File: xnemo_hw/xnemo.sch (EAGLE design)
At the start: 13 parts, among them J1 MICRO_USB_B_RECEPT, U1 LTC4O88, U2 L3GD20, U3 STM32F405RG, U5 HMC5883L, U6 ADXL345, X1 TXC_7A_XTAL

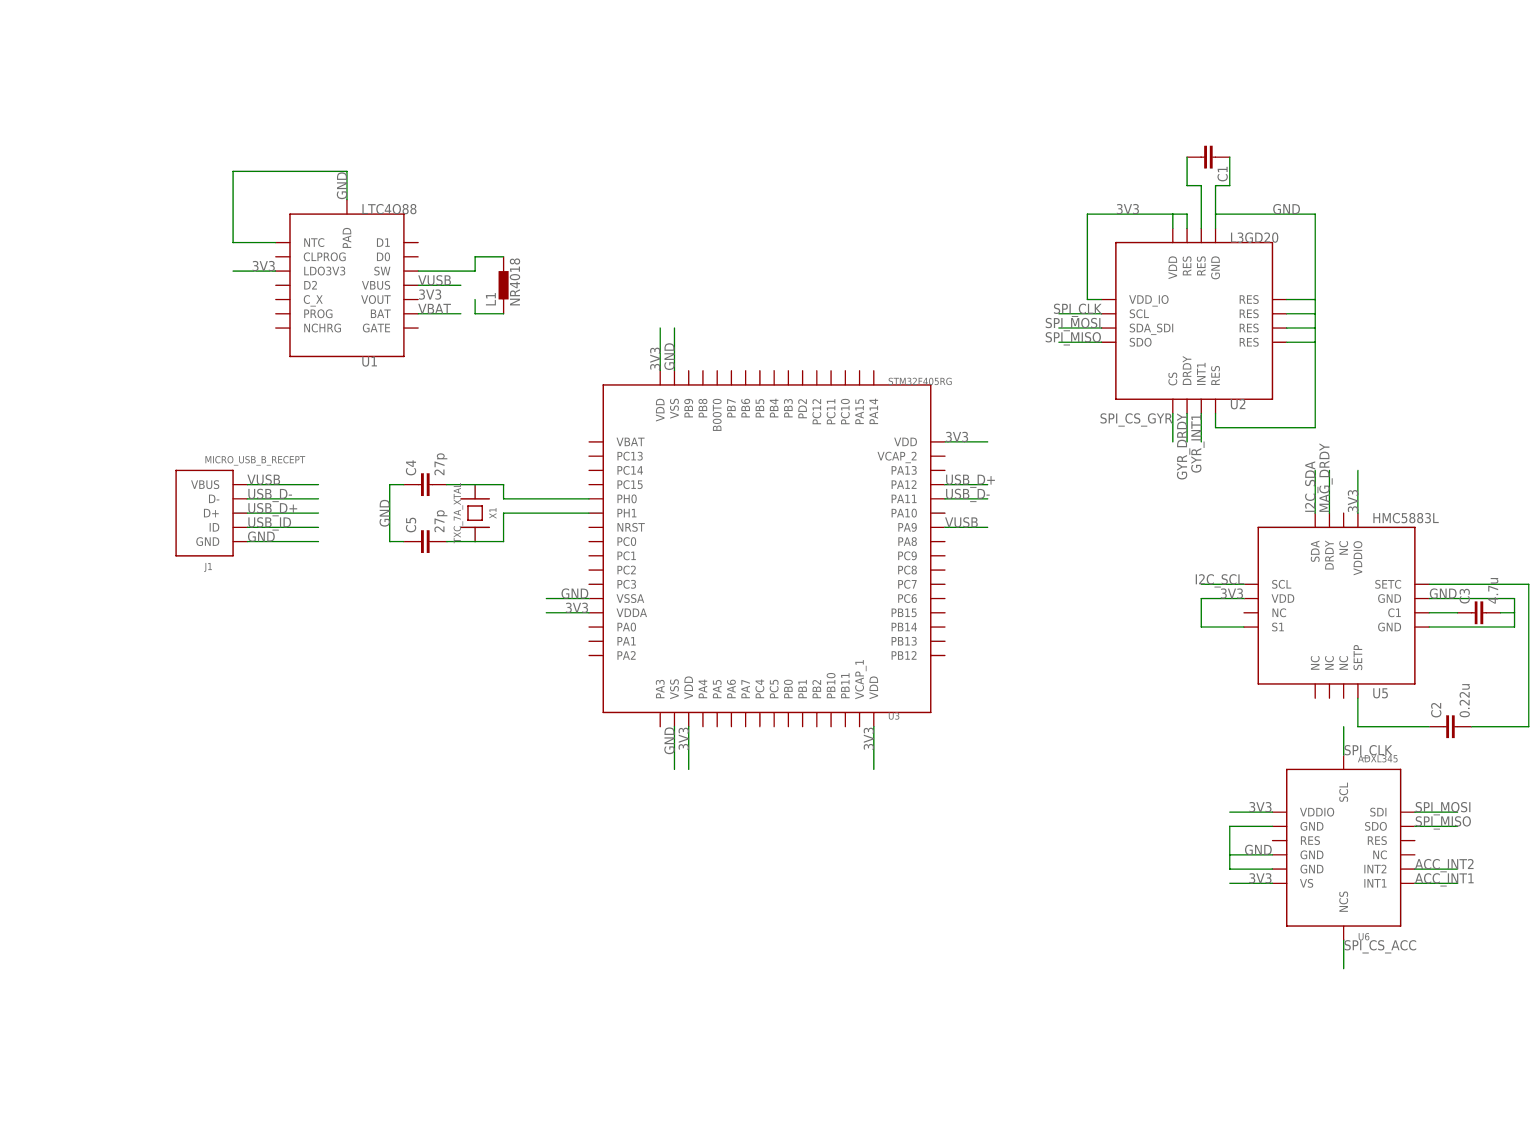
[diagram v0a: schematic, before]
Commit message: Updated schematic to all essential connections, started board to make smarter pin selections by including routing considerations
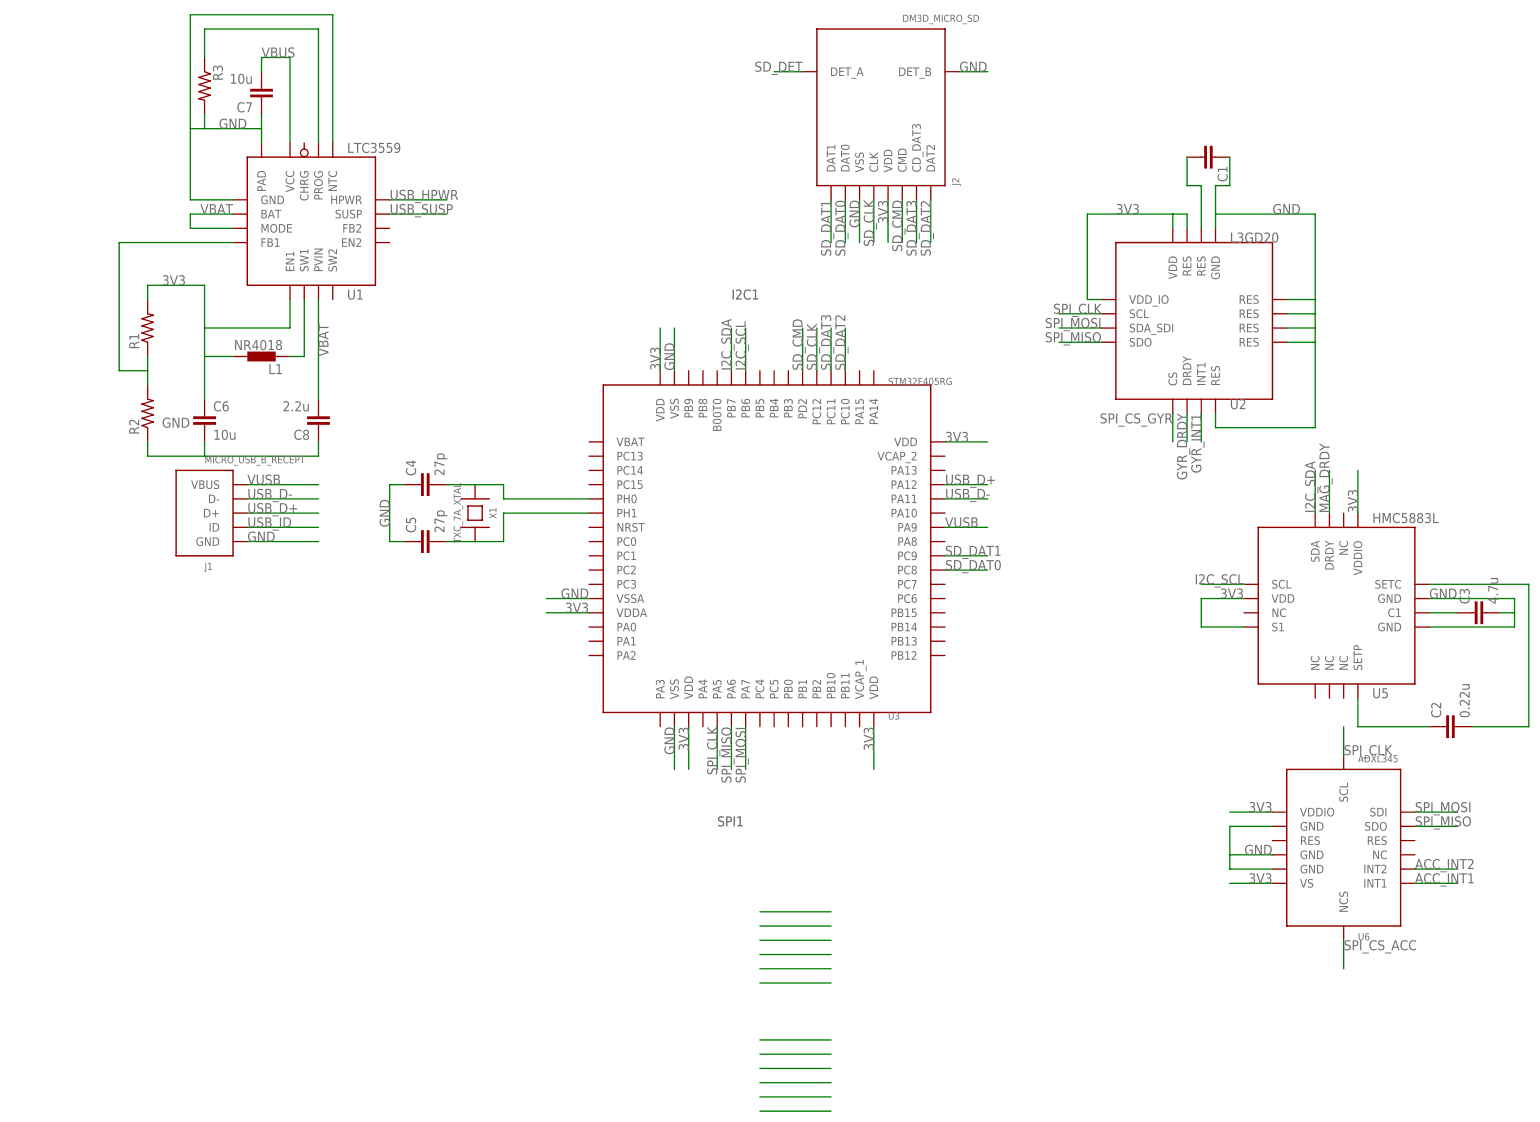
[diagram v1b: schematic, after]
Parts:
- added C6, C7: 10u, resistor:C-EUC0805
- added C8: 2.2u, resistor:C-EUC0805
- added J2: DM3D_MICRO_SD, xnemo:DM3D_MICRO_SD
- added R1, R2, R3: (no value), resistor:R-US_R0402
- U1: value LTC4O88 -> LTC3559; device xnemo:LTC4O88 -> xnemo:LTC3559
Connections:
- removed net SW: L1.2, U1.SW
- new net BUCK_FB1: R1.1, R2.2, U1.FB1
- new net BUCK_SW1: L1.1, U1.SW1
- new net N$1: R3.1, U1.PROG
- new net SD_CLK: J2.CLK, U3.PC12
- new net SD_CMD: J2.CMD, U3.PD2
- new net SD_DAT0: J2.DAT0, U3.PC8
- new net SD_DAT1: J2.DAT1, U3.PC9
- new net SD_DAT2: J2.DAT2, U3.PC10
- new net SD_DAT3: J2.CD_DAT3, U3.PC11
- new net SD_DET: J2.DET_A
- new net USB_HPWR: U1.HPWR
- new net USB_SUSP: U1.SUSP
- new net VBUS: C7.2, U1.VCC
- net 3V3: now also C6.1, J2.VDD, L1.2, R1.2, U1.EN1; no longer L1.1, U1.LDO3V3
- net GND: now also C6.2, C7.1, C8.1, J2.DET_B, J2.VSS, R2.1, R3.2, U1.GND
- net I2C_SCL: now also U3.PB6
- net I2C_SDA: now also U3.PB7
- net SPI_CLK: now also U3.PA5
- net SPI_MISO: now also U3.PA6
- net SPI_MOSI: now also U3.PA7
- net VBAT: now also C8.2, U1.MODE, U1.PVIN
- net VUSB: no longer U1.VBUS
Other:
- note added: "I2C1"
- note added: "SPI1"
- moved on the sheet: L1

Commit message: Updated some little things and added JTAG header
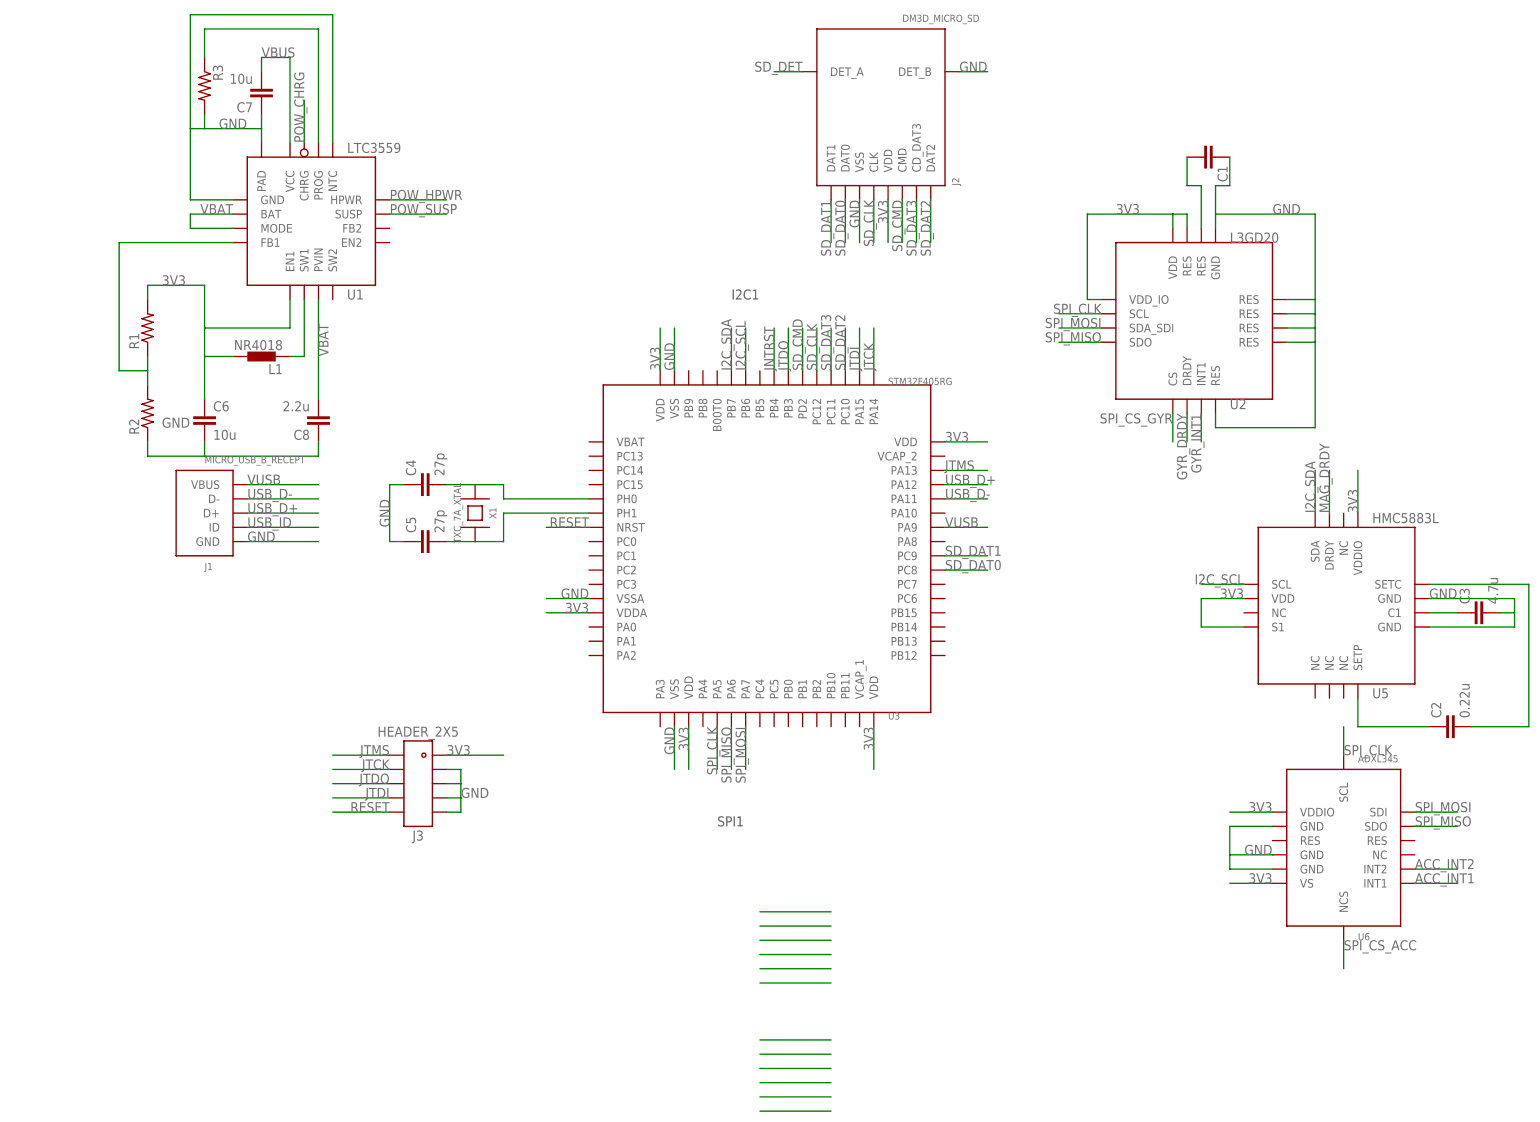
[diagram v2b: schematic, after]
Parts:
- added J3: HEADER_2X5, xnemo:HEADER_2X5
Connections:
- net USB_HPWR renamed POW_HPWR
- net USB_SUSP renamed POW_SUSP
- new net JNTRST: U3.PB4
- new net JTCK: J3.4, U3.PA14
- new net JTDI: J3.8, U3.PA15
- new net JTDO: J3.6, U3.PB3
- new net JTMS: J3.2, U3.PA13
- new net POW_CHRG: U1.CHRG
- new net RESET: J3.10, U3.NRST
- net 3V3: now also J3.1
- net GND: now also J3.3, J3.5, J3.7, J3.9

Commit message: Started bord
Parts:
- added C10, C11, C12, C9: 2.2u, resistor:C-EUC0603
- C4, C5: device resistor:C-EUC0603 -> resistor:C-EUC0402
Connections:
- net N$5 renamed GYR_RES
- removed net VBUS: C7.2, U1.VCC
- new net N$17: C10.1, U3.VCAP_1
- new net N$5: C11.1, U3.VCAP_2
- net 3V3: now also C12.1, C9.2
- net ACC_INT1: now also U3.PB1
- net ACC_INT2: now also U3.PB0
- net GND: now also C10.2, C11.2, C12.2, C9.1
- net GYR_DRDY: now also U3.PB13
- net GYR_INT1: now also U3.PB12
- net POW_CHRG: now also U3.PB2
- net POW_HPWR: now also U3.PB11
- net POW_SUSP: now also U3.PB10
- net SPI_CS_ACC: now also U3.PC5
- net SPI_CS_GYR: now also U3.PB14
- net VUSB: now also C7.2, U1.VCC
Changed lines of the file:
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@@
 <part name="J1" library="xnemo" deviceset="MICRO_USB_B_RECEPT" device=""/>
 <part name="X1" library="xnemo" deviceset="TXC_7A_XTAL" device=""/>
-<part name="C4" library="resistor" deviceset="C-EU" device="C0603" value="27p"/>
-<part name="C5" library="resistor" deviceset="C-EU" device="C0603" value="27p"/>
+<part name="C4" library="resistor" deviceset="C-EU" device="C0402" value="27p"/>
+<part name="C5" library="resistor" deviceset="C-EU" device="C0402" value="27p"/>
 <part name="U1" library="xnemo" deviceset="LTC3559" device=""/>
 <part name="C6" library="resistor" deviceset="C-EU" device="C0805" value="10u"/>
@@
 <part name="J3" library="xnemo" deviceset="HEADER_2X5" device=""/>
 <part name="U2" library="xnemo" deviceset="L3GD20" device=""/>
+<part name="C9" library="resistor" deviceset="C-EU" device="C0603" value="2.2u"/>
+<part name="C10" library="resistor" deviceset="C-EU" device="C0603" value="2.2u"/>
+<part name="C11" library="resistor" deviceset="C-EU" device="C0603" value="2.2u"/>
+<part name="C12" library="resistor" deviceset="C-EU" device="C0603" value="2.2u"/>
 </parts>
 <sheets>
@@
 <plain>
 <text x="20.32" y="-25.4" size="1.778" layer="97">SPI1</text>
-<text x="22.86" y="68.58" size="1.778" layer="97">I2C1</text>
+<text x="22.86" y="71.12" size="1.778" layer="97">I2C1</text>
 </plain>
 <instances>
@@
 <instance part="J3" gate="G$1" x="-33.02" y="-17.78"/>
 <instance part="U2" gate="G$1" x="104.14" y="66.04"/>
+<instance part="C9" gate="G$1" x="-17.78" y="15.24"/>
+<instance part="C10" gate="G$1" x="45.72" y="-17.78"/>
+<instance part="C11" gate="G$1" x="71.12" y="40.64" rot="R90"/>
+<instance part="C12" gate="G$1" x="10.16" y="66.04" rot="R90"/>
 </instances>
 <busses>
@@
 <wire x1="-2.54" y1="12.7" x2="-10.16" y2="12.7" width="0.1524" layer="91"/>
 <label x="-2.54" y="12.7" size="1.778" layer="95" rot="MR0"/>
+<pinref part="C9" gate="G$1" pin="2"/>
+<wire x1="-17.78" y1="10.16" x2="-10.16" y2="10.16" width="0.1524" layer="91"/>
+<wire x1="-10.16" y1="10.16" x2="-10.16" y2="12.7" width="0.1524" layer="91"/>
 </segment>
 <segment>
@@
 <wire x1="10.16" y1="55.88" x2="10.16" y2="63.5" width="0.1524" layer="91"/>
 <label x="10.16" y="55.88" size="1.778" layer="95" rot="R90"/>
+<pinref part="C12" gate="G$1" pin="1"/>
+<wire x1="10.16" y1="63.5" x2="7.62" y2="63.5" width="0.1524" layer="91"/>
+<wire x1="7.62" y1="63.5" x2="7.62" y2="66.04" width="0.1524" layer="91"/>
 </segment>
 <segment>
@@
 <wire x1="-2.54" y1="15.24" x2="-10.16" y2="15.24" width="0.1524" layer="91"/>
 <label x="-2.54" y="15.24" size="1.778" layer="95" rot="MR0"/>
+<wire x1="-10.16" y1="15.24" x2="-10.16" y2="17.78" width="0.1524" layer="91"/>
+<pinref part="C9" gate="G$1" pin="1"/>
+<wire x1="-10.16" y1="17.78" x2="-17.78" y2="17.78" width="0.1524" layer="91"/>
 </segment>
 <segment>
@@
 <wire x1="12.7" y1="55.88" x2="12.7" y2="63.5" width="0.1524" layer="91"/>
 <label x="12.7" y="55.88" size="1.778" layer="95" rot="R90"/>
+<pinref part="C12" gate="G$1" pin="2"/>
+<wire x1="12.7" y1="63.5" x2="15.24" y2="63.5" width="0.1524" layer="91"/>
+<wire x1="15.24" y1="63.5" x2="15.24" y2="66.04" width="0.1524" layer="91"/>
 </segment>
 <segment>
@@
 <label x="-25.4" y="-20.32" size="1.778" layer="95"/>
 </segment>
-</net>
-<net name="N$5" class="0">
+<segment>
+<pinref part="C10" gate="G$1" pin="2"/>
+<wire x1="45.72" y1="-22.86" x2="45.72" y2="-25.4" width="0.1524" layer="91"/>
+<label x="45.72" y="-22.86" size="1.778" layer="95" rot="MR270"/>
+</segment>
+<segment>
+<pinref part="C11" gate="G$1" pin="2"/>
+<wire x1="76.2" y1="40.64" x2="78.74" y2="40.64" width="0.1524" layer="91"/>
+<label x="76.2" y="40.64" size="1.778" layer="95"/>
+</segment>
+</net>
+<net name="GYR_RES" class="0">
 <segment>
 <pinref part="C1" gate="G$1" pin="2"/>
@@
 <label x="132.08" y="-45.72" size="1.778" layer="95" rot="MR180"/>
 </segment>
+<segment>
+<pinref part="U3" gate="G$1" pin="PC5"/>
+<wire x1="30.48" y1="-7.62" x2="30.48" y2="-15.24" width="0.1524" layer="91"/>
+<label x="30.48" y="-7.62" size="1.778" layer="95" rot="MR270"/>
+</segment>
 </net>
 <net name="SPI_CS_GYR" class="0">
@@
 <pinref part="U2" gate="G$1" pin="CS"/>
 </segment>
+<segment>
+<pinref part="U3" gate="G$1" pin="PB14"/>
+<wire x1="60.96" y1="10.16" x2="68.58" y2="10.16" width="0.1524" layer="91"/>
+<label x="60.96" y="10.16" size="1.778" layer="95"/>
+</segment>
 </net>
 <net name="ACC_INT1" class="0">
@@
 <label x="144.78" y="-35.56" size="1.778" layer="95"/>
 </segment>
+<segment>
+<pinref part="U3" gate="G$1" pin="PB1"/>
+<wire x1="35.56" y1="-7.62" x2="35.56" y2="-15.24" width="0.1524" layer="91"/>
+<label x="35.56" y="-7.62" size="1.778" layer="95" rot="MR270"/>
+</segment>
 </net>
 <net name="ACC_INT2" class="0">
@@
 <label x="144.78" y="-33.02" size="1.778" layer="95"/>
 </segment>
+<segment>
+<pinref part="U3" gate="G$1" pin="PB0"/>
+<wire x1="33.02" y1="-7.62" x2="33.02" y2="-15.24" width="0.1524" layer="91"/>
+<label x="33.02" y="-7.62" size="1.778" layer="95" rot="MR270"/>
+</segment>
 </net>
 <net name="I2C_SDA" class="0">
@@
 <wire x1="129.54" y1="30.48" x2="129.54" y2="38.1" width="0.1524" layer="91"/>
 <label x="129.54" y="30.48" size="1.778" layer="95" rot="R90"/>
+<wire x1="27.94" y1="55.88" x2="27.94" y2="63.5" width="0.1524" layer="91"/>
+<label x="27.94" y="55.88" size="1.778" layer="95" rot="R90"/>
 </segment>
 </net>
@@
 <pinref part="U2" gate="G$1" pin="DRDY"/>
 </segment>
+<segment>
+<pinref part="U3" gate="G$1" pin="PB13"/>
+<wire x1="60.96" y1="7.62" x2="68.58" y2="7.62" width="0.1524" layer="91"/>
+<label x="60.96" y="7.62" size="1.778" layer="95"/>
+</segment>
 </net>
 <net name="GYR_INT1" class="0">
@@
 <label x="106.68" y="48.26" size="1.778" layer="95" rot="MR270"/>
 <pinref part="U2" gate="G$1" pin="INT1"/>
+</segment>
+<segment>
+<pinref part="U3" gate="G$1" pin="PB12"/>
+<wire x1="60.96" y1="5.08" x2="68.58" y2="5.08" width="0.1524" layer="91"/>
+<label x="60.96" y="5.08" size="1.778" layer="95"/>
 </segment>
 </net>
@@
 <wire x1="60.96" y1="27.94" x2="68.58" y2="27.94" width="0.1524" layer="91"/>
 <label x="60.96" y="27.94" size="1.778" layer="95"/>
+</segment>
+<segment>
+<pinref part="U1" gate="G$1" pin="VCC"/>
+<wire x1="-55.88" y1="96.52" x2="-55.88" y2="111.76" width="0.1524" layer="91"/>
+<wire x1="-55.88" y1="111.76" x2="-60.96" y2="111.76" width="0.1524" layer="91"/>
+<pinref part="C7" gate="G$1" pin="2"/>
+<wire x1="-60.96" y1="111.76" x2="-60.96" y2="109.22" width="0.1524" layer="91"/>
+<label x="-60.96" y="111.76" size="1.778" layer="95"/>
 </segment>
 </net>
@@
 </segment>
 </net>
-<net name="VBUS" class="0">
-<segment>
-<pinref part="U1" gate="G$1" pin="VCC"/>
-<wire x1="-55.88" y1="96.52" x2="-55.88" y2="111.76" width="0.1524" layer="91"/>
-<wire x1="-55.88" y1="111.76" x2="-60.96" y2="111.76" width="0.1524" layer="91"/>
-<pinref part="C7" gate="G$1" pin="2"/>
-<wire x1="-60.96" y1="111.76" x2="-60.96" y2="109.22" width="0.1524" layer="91"/>
-<label x="-60.96" y="111.76" size="1.778" layer="95"/>
-</segment>
-</net>
 <net name="POW_SUSP" class="0">
 <segment>
@@
 <label x="-38.1" y="83.82" size="1.778" layer="95"/>
 </segment>
+<segment>
+<pinref part="U3" gate="G$1" pin="PB10"/>
+<wire x1="40.64" y1="-7.62" x2="40.64" y2="-15.24" width="0.1524" layer="91"/>
+<label x="40.64" y="-7.62" size="1.778" layer="95" rot="MR270"/>
+</segment>
 </net>
 <net name="POW_HPWR" class="0">
@@
 <wire x1="-38.1" y1="86.36" x2="-27.94" y2="86.36" width="0.1524" layer="91"/>
 <label x="-38.1" y="86.36" size="1.778" layer="95"/>
+</segment>
+<segment>
+<pinref part="U3" gate="G$1" pin="PB11"/>
+<wire x1="43.18" y1="-7.62" x2="43.18" y2="-15.24" width="0.1524" layer="91"/>
+<label x="43.18" y="-7.62" size="1.778" layer="95" rot="MR270"/>
 </segment>
 </net>
@@
 <label x="-53.34" y="96.52" size="1.778" layer="95" rot="R90"/>
 </segment>
+<segment>
+<pinref part="U3" gate="G$1" pin="PB2"/>
+<wire x1="38.1" y1="-7.62" x2="38.1" y2="-15.24" width="0.1524" layer="91"/>
+<label x="38.1" y="-7.62" size="1.778" layer="95" rot="MR270"/>
+</segment>
 </net>
 <net name="JTMS" class="0">
@@
 </segment>
 </net>
+<net name="N$5" class="0">
+<segment>
+<pinref part="U3" gate="G$1" pin="VCAP_2"/>
+<pinref part="C11" gate="G$1" pin="1"/>
+<wire x1="60.96" y1="40.64" x2="68.58" y2="40.64" width="0.1524" layer="91"/>
+</segment>
+</net>
+<net name="N$17" class="0">
+<segment>
+<pinref part="C10" gate="G$1" pin="1"/>
+<pinref part="U3" gate="G$1" pin="VCAP_1"/>
+<wire x1="45.72" y1="-15.24" x2="45.72" y2="-7.62" width="0.1524" layer="91"/>
+</segment>
+</net>
